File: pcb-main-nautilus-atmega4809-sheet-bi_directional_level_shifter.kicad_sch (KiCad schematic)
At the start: 3 parts, among them Q1 BSS138PW,115

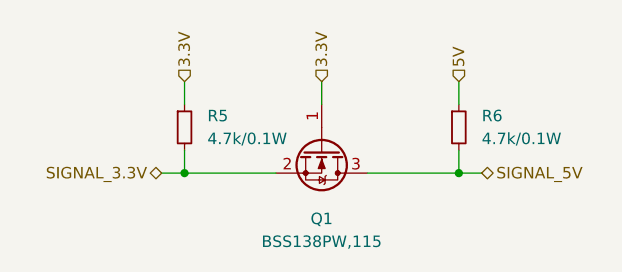
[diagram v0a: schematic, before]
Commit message: Connect root sheet
Supports #2.
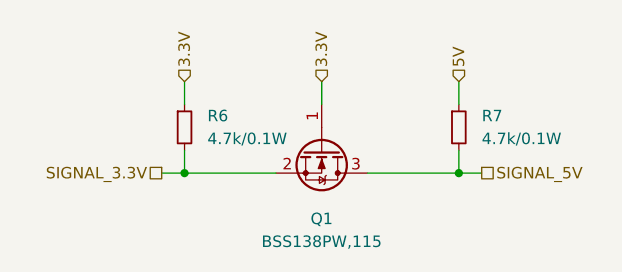
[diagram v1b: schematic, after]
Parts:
- renumbered R5 to R6, R6 to R7
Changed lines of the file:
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@@
     (stroke (width 0) (type default) (color 0 0 0 0))
   )
-  (hierarchical_label "SIGNAL_3.3V" (shape bidirectional) (at 121.92 110.49 180)
+  (hierarchical_label "SIGNAL_3.3V" (shape passive) (at 121.92 110.49 180)
     (effects (font (size 1.27 1.27)) (justify right))
   )
@@
     (effects (font (size 1.27 1.27)) (justify left))
   )
-  (hierarchical_label "SIGNAL_5V" (shape bidirectional) (at 157.48 110.49 0)
+  (hierarchical_label "SIGNAL_5V" (shape passive) (at 157.48 110.49 0)
     (effects (font (size 1.27 1.27)) (justify left))
   )
   (symbol (lib_id "Device:R_Small") (at 154.94 105.41 0) (unit 1)
     (in_bom yes) (on_board yes) (fields_autoplaced)
-    (property "Reference" "R6" (id 0) (at 157.48 104.1399 0)
+    (property "Reference" "R7" (id 0) (at 157.48 104.1399 0)
       (effects (font (size 1.27 1.27)) (justify left))
     )
@@
   (symbol (lib_id "Device:R_Small") (at 124.46 105.41 0) (unit 1)
     (in_bom yes) (on_board yes) (fields_autoplaced)
-    (property "Reference" "R5" (id 0) (at 127 104.1399 0)
+    (property "Reference" "R6" (id 0) (at 127 104.1399 0)
       (effects (font (size 1.27 1.27)) (justify left))
     )
